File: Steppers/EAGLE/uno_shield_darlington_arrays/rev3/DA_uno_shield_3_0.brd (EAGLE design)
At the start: 54 x 59.7 mm, 16 parts

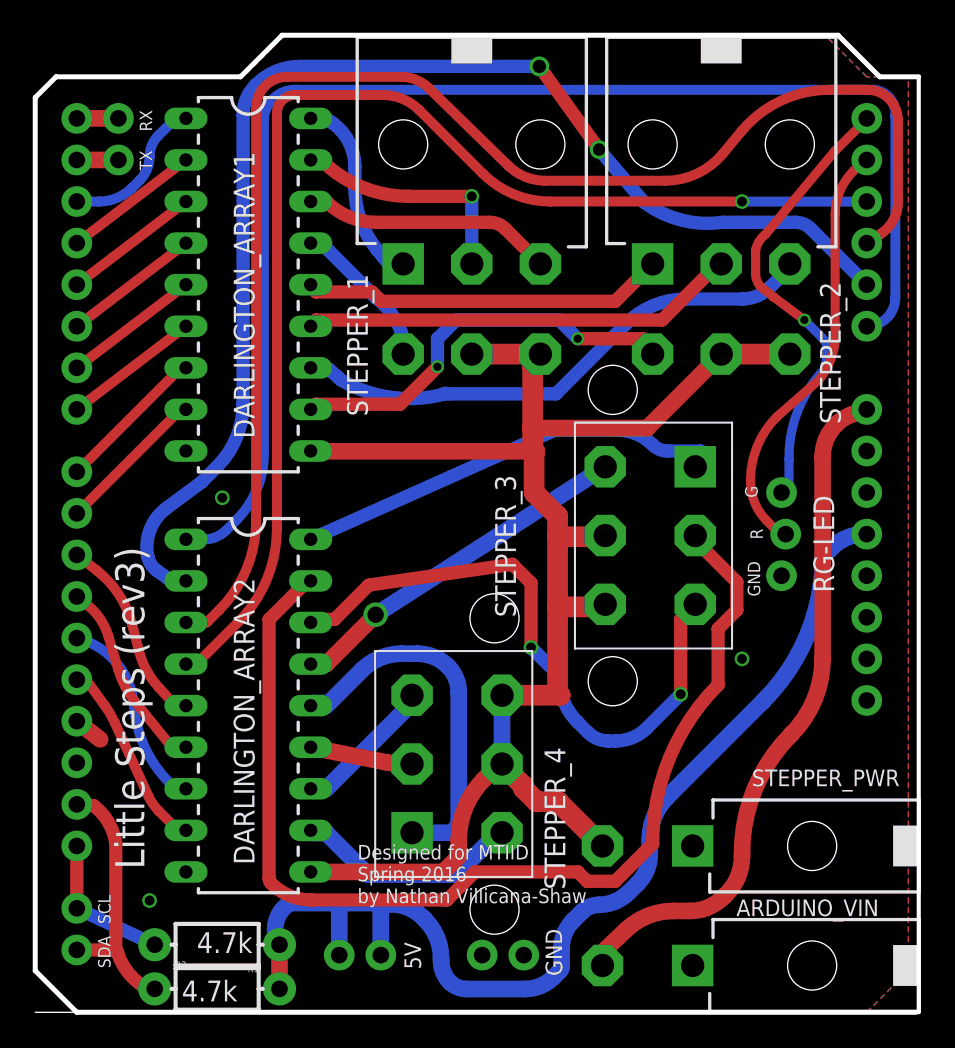
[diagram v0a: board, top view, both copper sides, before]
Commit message: revised stepper uno shield for second time
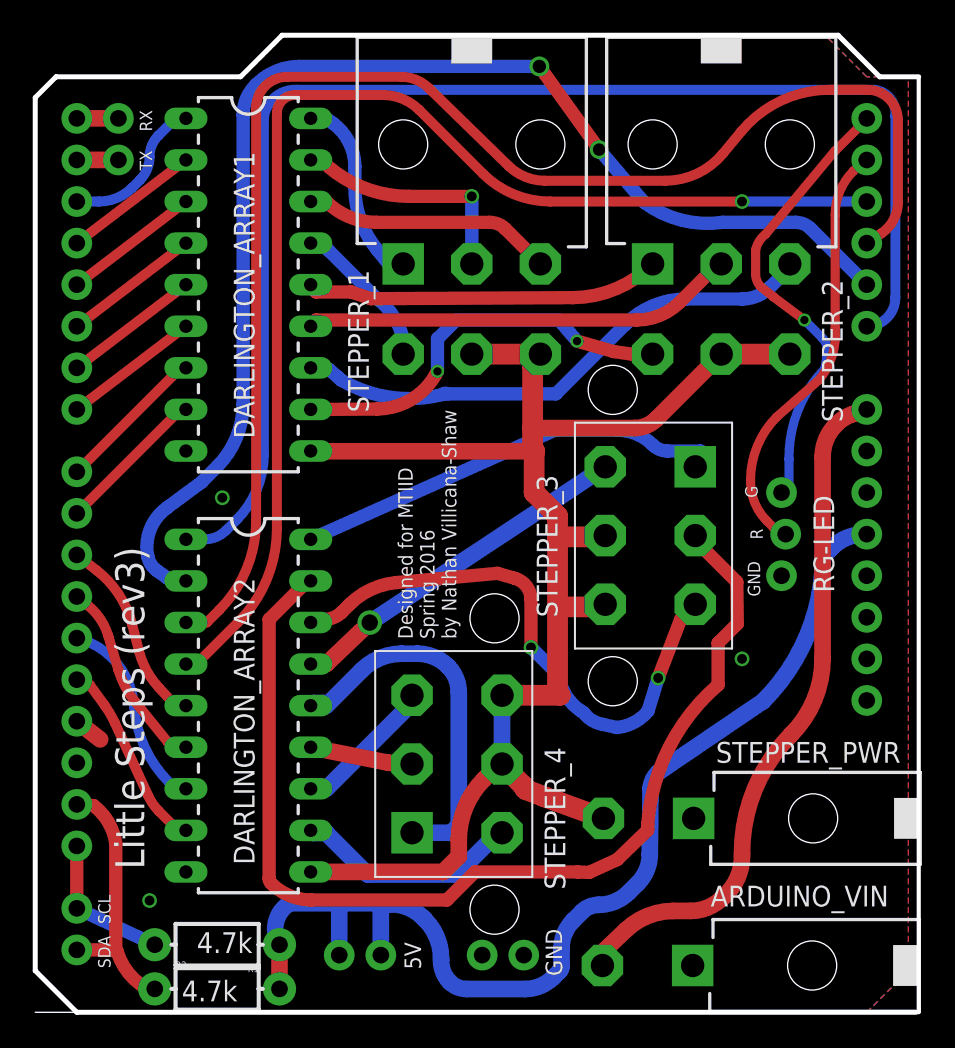
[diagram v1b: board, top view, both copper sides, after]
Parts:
- moved STEPPER_PWR 1.69 mm to (40.2, 11.8)
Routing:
- net N$42: track 37.9 -> 34.5 mm
- net VCC: track 95.4 -> 94.2 mm
- net N$41: track 66.2 -> 65.0 mm
- net 5V: track 65.8 -> 66.7 mm
- net N$1: track 22.3 -> 21.6 mm
